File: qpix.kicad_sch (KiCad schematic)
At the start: 91 parts, among them J1 Conn_01x40, J10 VC, J13 DigReset, J2 Conn_01x09, J3 Conn_02x03, J4 Conn_02x03, J5 SPI, J6 Conn_02x03, J8 Conn_02x03, J9 Conn_Coaxial_Power, Q1 Q_NMOS_GSD, Q2 Q_NMOS_GSD, Q3 Q_NMOS_GSD, Q4 Q_NMOS_GSD, U1 qpix_digital

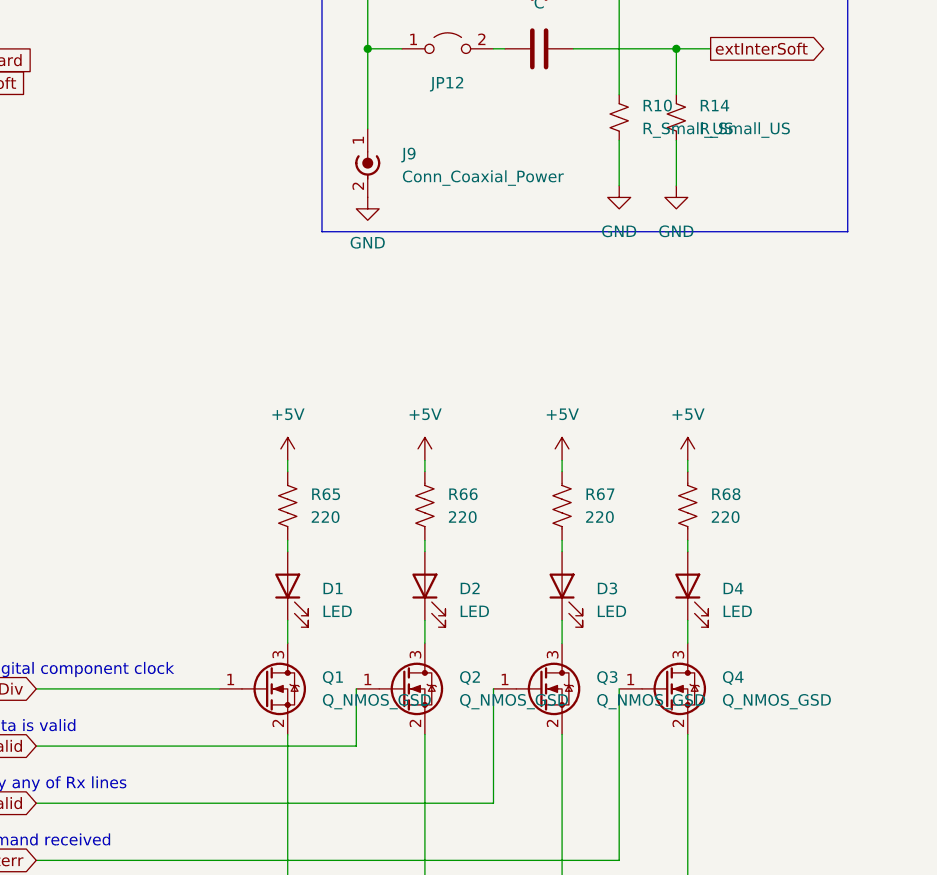
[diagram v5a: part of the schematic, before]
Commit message: trying to reroute new cob footprint
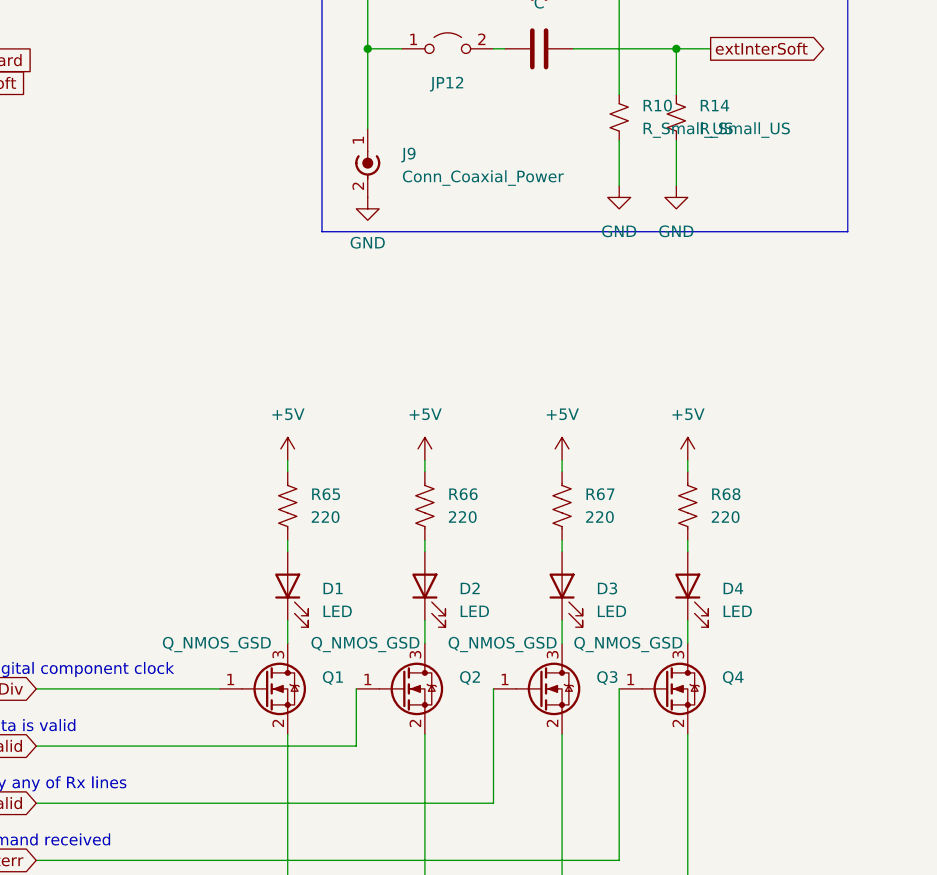
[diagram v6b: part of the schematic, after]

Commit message: add part values for missed ones
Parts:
- C10, C8: value C -> 220 nF
- C11: value C -> 2 nF
- C12, C24: value C -> 22uF
- C13, C14: value C -> 2uF
- C15, C16: value C -> 220nF
- C17, C18: value C -> 2nF
- C22, C23: value C -> 100nF
- C4, C5: value C -> 22 uF
- C6, C7: value C -> 2.2 uF
- Q1, Q2, Q3, Q4: value Q_NMOS_GSD -> AO7400
- R1, R11, R12, R2, R3, R4, R5: value R_US -> 10k
- R10, R14: value R_Small_US -> 22k
- R6: value (none) -> 10k
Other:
- note added: "10k-22k"
- note added: "2 22 uF 2 2.2 uf 2 220 nf 2 2nf"
- note removed: "Kurtis: As far as resistor sizes, I would use at least 0603 for all those resistors and capacitors"
- note removed: "Kurtis: I would spec those as 1% 100 Ohm."

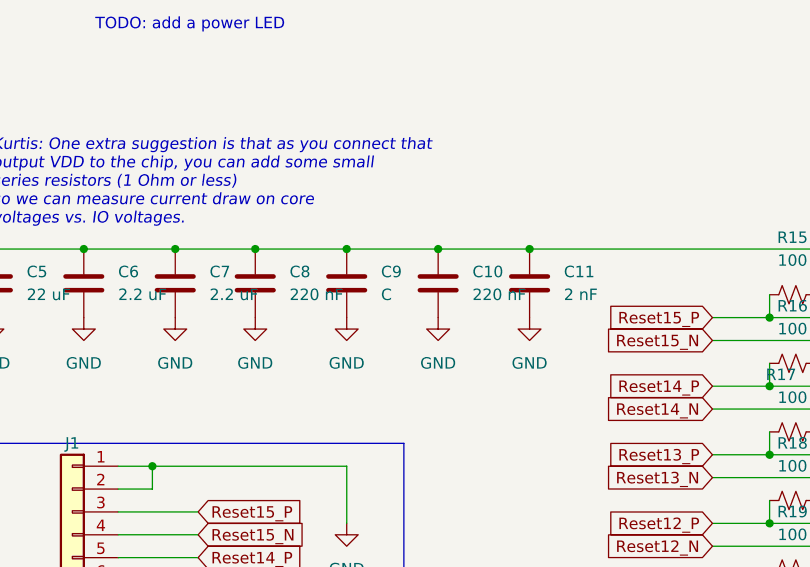
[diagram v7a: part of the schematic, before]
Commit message: fix external clock input
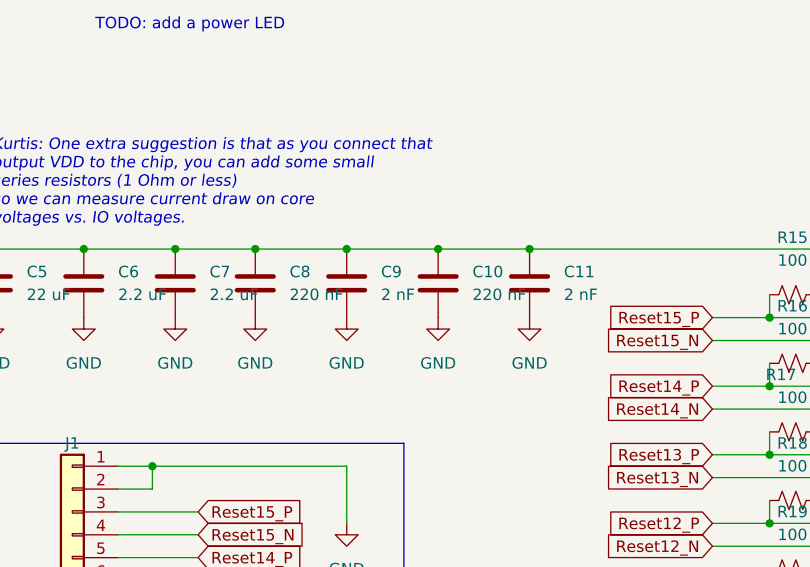
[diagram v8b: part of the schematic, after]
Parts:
- C9: value C -> 2 nF
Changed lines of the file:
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@@
   (symbol (lib_id "Device:C") (at 63.5 96.52 0) (unit 1)
     (in_bom yes) (on_board yes) (dnp no) (fields_autoplaced)
-    (property "Reference" "C9" (at 67.31 95.2499 0)
+    (property "Reference" "C9" (at 67.31 95.25 0)
       (effects (font (size 1.27 1.27)) (justify left))
     )
-    (property "Value" "C" (at 67.31 97.7899 0)
+    (property "Value" "2 nF" (at 67.31 97.79 0)
       (effects (font (size 1.27 1.27)) (justify left))
     )
